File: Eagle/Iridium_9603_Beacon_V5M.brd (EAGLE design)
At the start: 78 x 121 mm, 111 parts, among them CON4 uFL, J1 SS4-10-3.50-X-D, Q1 DMG3415U-7, Q2 DMG3415U-7, Q3 DMG3415U-7, Q4 DMG3415U-7, Q5 2N2222, U1 MCP111T-240E/TT, U2 SPX3819-3.3, U3 LTC3225EDDB#TRMPBF, U4 MPL3115A2LGA8, U5 ATSAMD21G18_QFN, U53 7101K2AV2QE, U6 MAX-M8, U7 LT1634-1,25BMCMS8, X1 32.768

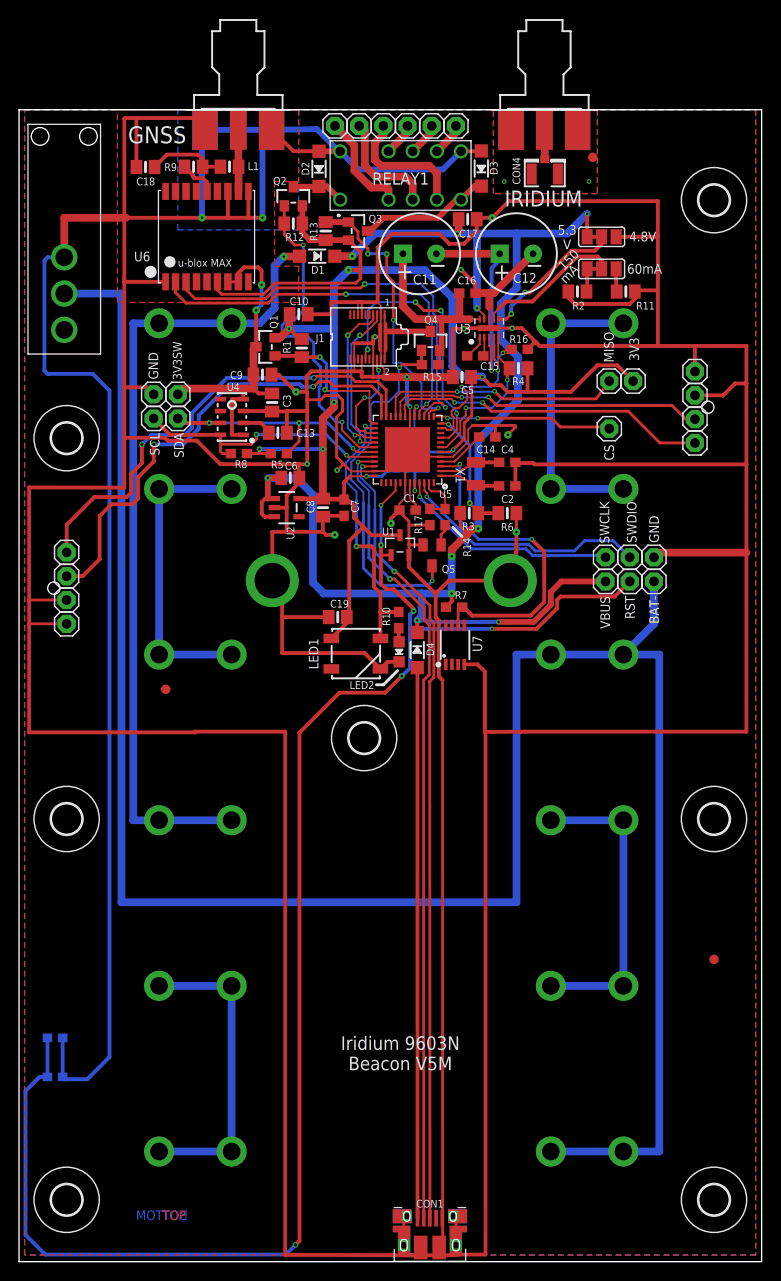
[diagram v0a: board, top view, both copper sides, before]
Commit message: starting operational Iridium9603NBeacon_V5M arduiono code
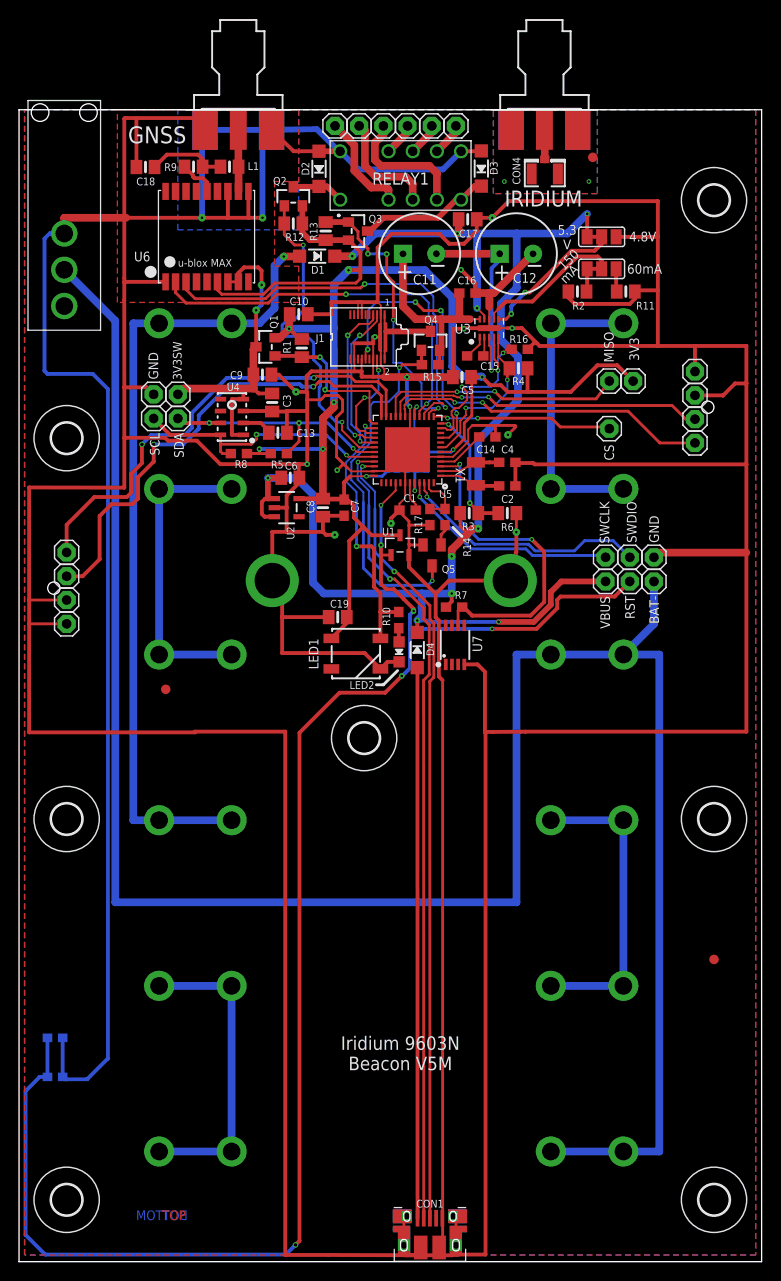
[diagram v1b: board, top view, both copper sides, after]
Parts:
- moved U53 2.50 mm to (19.8, 121.5)
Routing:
- net N$15: track 225.1 -> 224.4 mm
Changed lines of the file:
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@@
 <drawing>
 <settings>
-<setting alwaysvectorfont="no"/>
+<setting alwaysvectorfont="yes"/>
 <setting keepoldvectorfont="yes"/>
 <setting verticaltext="up"/>
@@
 </layers>
 <board>
-<fusionsync huburn="a.cGVyc29uYWw6dWUyY2Q5OTI4" projecturn="a.cGVyc29uYWw6dWUyY2Q5OTI4IzIwMTgxMjE0MTY1NTY1NzU2" f3durn="urn:adsk.wipprod:dm.lineage:w9AHYNf_Q9GseIxamkbaeA" pcbguid="954f3457-adb5-463a-954c-105c6e7f83b2" lastpulledtime="2018-12-29T03:57:47Z" lastsyncedchangeguid="a3efed41-22df-3280-2fd7-7d1e25b3e0f3"/>
+<fusionsync huburn="a.cGVyc29uYWw6dWUyY2Q5OTI4" projecturn="a.cGVyc29uYWw6dWUyY2Q5OTI4IzIwMTgxMjE0MTY1NTY1NzU2" f3durn="urn:adsk.wipprod:dm.lineage:w9AHYNf_Q9GseIxamkbaeA" pcbguid="954f3457-adb5-463a-954c-105c6e7f83b2" lastpulledtime="2018-12-29T03:57:47Z" lastsyncedchangeguid="7e7b2e13-171d-be95-e8c6-1b83e62745c9"/>
 <plain>
 <text x="29.99725" y="17.867" size="1.016" layer="1" font="vector" ratio="16">TOP</text>
@@
 <dimension x1="14.99" y1="136.07" x2="20" y2="60" x3="-34.1" y3="98.035" textsize="1.778" layer="51" dtype="vertical"/>
 <dimension x1="15.01" y1="136.09" x2="20" y2="20" x3="-53.4" y3="78.045" textsize="1.778" layer="51" dtype="vertical"/>
+<dimension x1="88" y1="125" x2="74.84" y2="136.05" x3="115.85" y3="130.525" textsize="1.778" layer="51" dtype="vertical"/>
+<dimension x1="88" y1="125" x2="88.21" y2="134.5" x3="130.4" y3="129.75" textsize="1.778" layer="51" dtype="vertical"/>
+<dimension x1="51.25" y1="68.5" x2="15" y2="134.5" x3="10.64" y3="101.5" textsize="1.778" layer="51" dtype="vertical"/>
+<dimension x1="51.25" y1="68.5" x2="15" y2="134.5" x3="33.125" y3="-15.09" textsize="1.778" layer="51" dtype="horizontal"/>
+<dimension x1="88" y1="125" x2="20" y2="100" x3="129.22" y3="112.5" textsize="1.778" layer="51" dtype="vertical"/>
+<dimension x1="88" y1="125" x2="88" y2="60" x3="140.58" y3="92.5" textsize="1.778" layer="51" dtype="vertical"/>
+<dimension x1="88" y1="125" x2="88" y2="20" x3="152.88" y3="72.5" textsize="1.778" layer="51" dtype="vertical"/>
 </plain>
 <attributes>
@@
 <element name="U$51" library="holes" library_urn="urn:adsk.eagle:library:237" package="3,2" package3d_urn="urn:adsk.eagle:package:14275/1" value="" x="88" y="125" smashed="yes"/>
 <element name="U$52" library="holes" library_urn="urn:adsk.eagle:library:237" package="3,2" package3d_urn="urn:adsk.eagle:package:14275/1" value="" x="20" y="100" smashed="yes"/>
-<element name="U53" library="argol-eagle-library" package="AV2_SPDT" value="7101K2AV2QE" x="19.75" y="119" smashed="yes" rot="R180"/>
+<element name="U53" library="argol-eagle-library" package="AV2_SPDT" value="7101K2AV2QE" x="19.75" y="121.5" smashed="yes" rot="R180"/>
 <element name="FD3" library="SparkFun-Aesthetics" package="FIDUCIAL-1X2" value="FIDUCIAL1X2" x="88" y="45.25" smashed="yes"/>
 <element name="U$2" library="holes" library_urn="urn:adsk.eagle:library:237" package="3,2" package3d_urn="urn:adsk.eagle:package:14275/1" value="" x="51.25" y="68.5" smashed="yes"/>
@@
 <contactref element="U53" pad="P$1"/>
 <wire x1="26.25" y1="123.15" x2="19.75" y2="123.15" width="0.8128" layer="1"/>
-<wire x1="19.75" y1="123.15" x2="19.75" y2="119" width="0.8128" layer="1"/>
+<wire x1="19.75" y1="123.15" x2="19.75" y2="121.5" width="0.8128" layer="1"/>
 <wire x1="91.4032" y1="105.75" x2="91.4032" y2="109.688" width="0.4064" layer="1"/>
 <wire x1="42.95975" y1="69.175" x2="42.95975" y2="14.20605625" width="0.4064" layer="1"/>
 <wire x1="42.95975" y1="14.20605625" x2="47.500646875" y2="14.20605625" width="0.4064" layer="1"/>
-<wire x1="19.75" y1="119" x2="18" y2="119" width="0.4064" layer="16"/>
-<wire x1="18" y1="119" x2="17.67075" y2="118.67075" width="0.4064" layer="16"/>
-<wire x1="17.67075" y1="118.67075" x2="17.67075" y2="107.07925" width="0.4064" layer="16"/>
+<wire x1="19.75" y1="121.5" x2="18.2824" y2="121.5" width="0.4064" layer="16"/>
+<wire x1="18.2824" y1="121.5" x2="18.23" y2="121.52" width="0.4064" layer="16"/>
+<wire x1="18.23" y1="121.52" x2="17.67075" y2="120.96075" width="0.4064" layer="16"/>
+<wire x1="17.67075" y1="120.96075" x2="17.67075" y2="107.07925" width="0.4064" layer="16"/>
 <wire x1="17.67075" y1="107.07925" x2="18" y2="106.75" width="0.4064" layer="16"/>
 <wire x1="18" y1="106.75" x2="22.75" y2="106.75" width="0.4064" layer="16"/>
-<wire x1="22.75" y1="106.75" x2="24.5" y2="105" width="0.4064" layer="16"/>
-<wire x1="24.5" y1="105" x2="24.5" y2="35" width="0.4064" layer="16"/>
+<wire x1="22.75" y1="106.75" x2="24.34" y2="105.16" width="0.4064" layer="16"/>
+<wire x1="24.34" y1="105.16" x2="24.34" y2="34.84" width="0.4064" layer="16"/>
 <wire x1="22.165" y1="32.665" x2="19.83" y2="32.665" width="0.4064" layer="16"/>
-<wire x1="24.5" y1="35" x2="22.165" y2="32.665" width="0.4064" layer="16"/>
+<wire x1="24.34" y1="34.84" x2="22.165" y2="32.665" width="0.4064" layer="16"/>
 <wire x1="19.83" y1="32.665" x2="19.585" y2="32.91" width="0.4064" layer="16"/>
 <wire x1="56.064" y1="103.30625" x2="56.06" y2="103.30225" width="0.2032" layer="1"/>
@@
 <wire x1="67.25" y1="51.25" x2="67.25" y2="77.271" width="0.8128" layer="16"/>
 <contactref element="U53" pad="P$2"/>
-<wire x1="19.75" y1="115.19" x2="25.75" y2="115.19" width="0.8128" layer="16"/>
-<wire x1="25.75" y1="51.25" x2="67.25" y2="51.25" width="0.8128" layer="16"/>
-<wire x1="25.75" y1="115.19" x2="25.75" y2="51.25" width="0.8128" layer="16"/>
+<wire x1="19.75" y1="117.69" x2="25.11" y2="112.33" width="0.8128" layer="16"/>
+<wire x1="25.11" y1="51.25" x2="67.25" y2="51.25" width="0.8128" layer="16"/>
+<wire x1="25.11" y1="112.33" x2="25.11" y2="51.25" width="0.8128" layer="16"/>
 <wire x1="81.69" y1="84.951" x2="81.69" y2="80.481" width="0.8128" layer="16"/>
 <wire x1="81.69" y1="80.481" x2="78.48" y2="77.271" width="0.8128" layer="16"/>

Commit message: Added diode to second battery pack
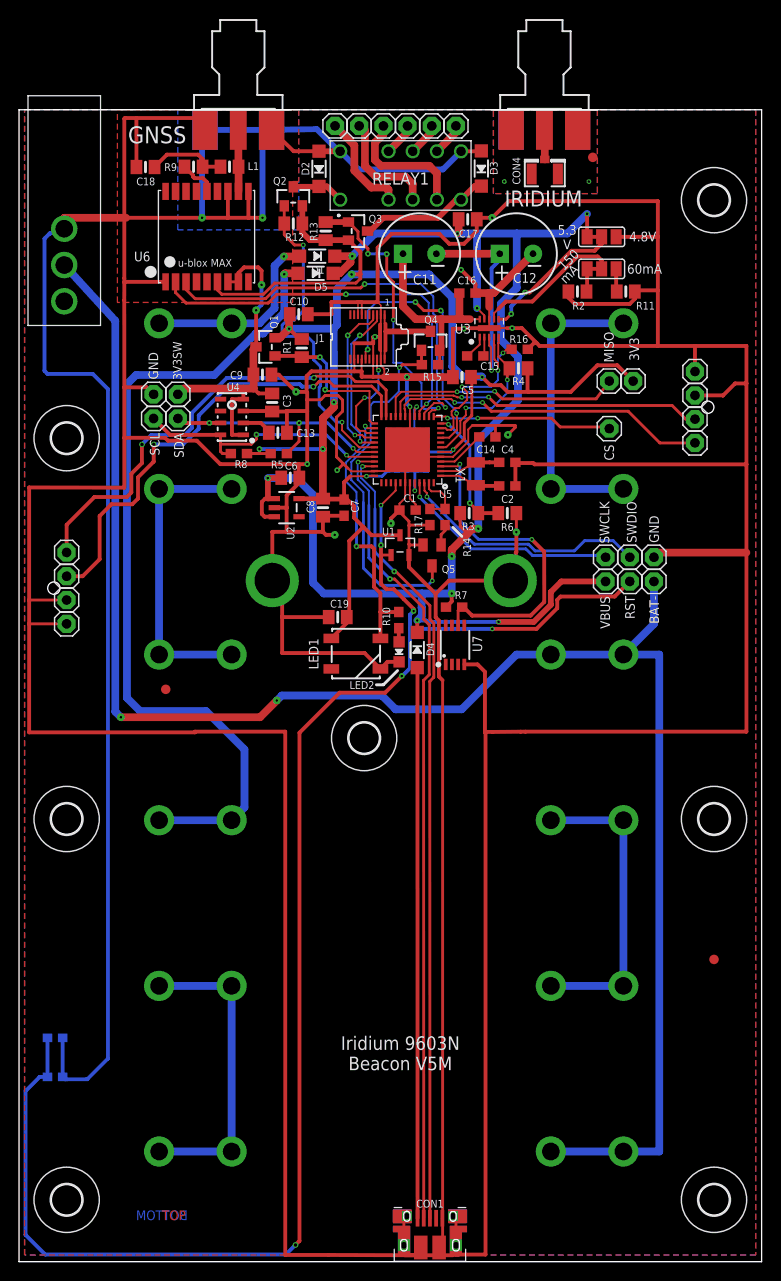
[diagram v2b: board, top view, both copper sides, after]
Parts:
- added D5: MBR120, microbuilder:SOD-123
- moved U53 0.50 mm to (19.8, 122.0)
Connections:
- new net VBAT1: BAT4.PWR@1, BAT4.PWR@2, D5.A
- net VBAT: no longer BAT4.PWR@1, BAT4.PWR@2
- net VBUS: now also D5.C
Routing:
- net VBAT1: track 0.00 -> 88.3 mm, vias 0 -> 1
- net VBAT: track 85.5 -> 20.3 mm
- net N$15: track 224.4 -> 182.9 mm, vias 0 -> 2
- net VBUS: track 152.5 -> 155.5 mm
- net +3V3: track 196.9 -> 195.7 mm
